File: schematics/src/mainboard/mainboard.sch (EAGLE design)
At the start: 44 parts, among them IC1 TL074P, IC2 TL074P

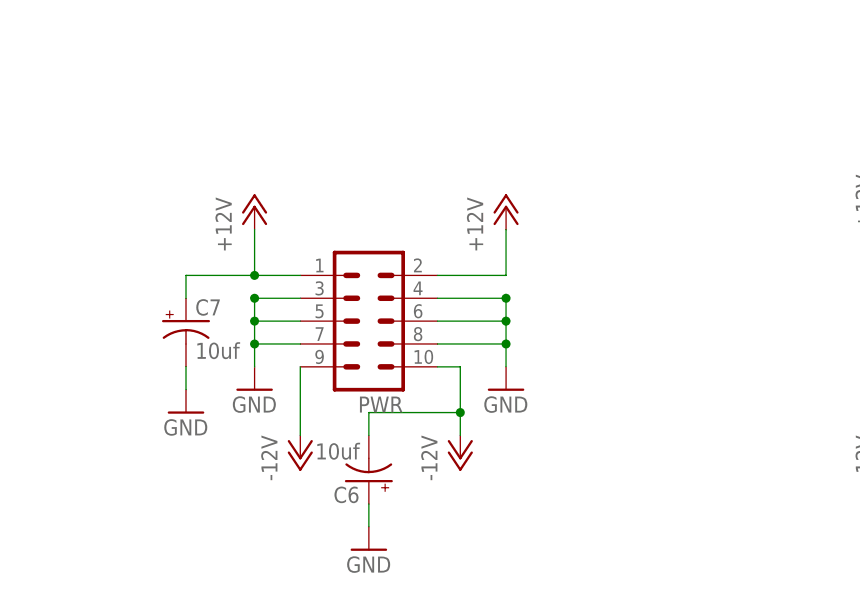
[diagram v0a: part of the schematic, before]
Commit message: Updated Schematics, Fixed Power Socket orientation
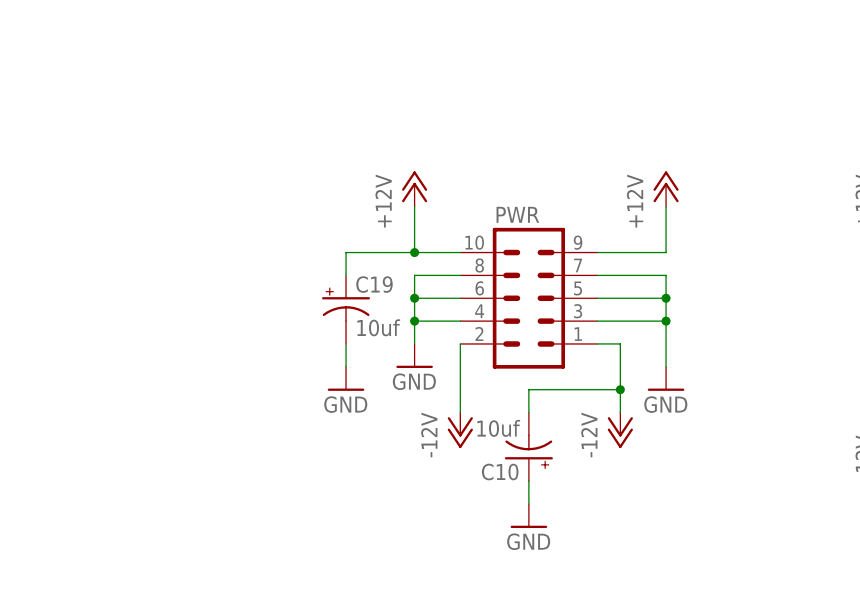
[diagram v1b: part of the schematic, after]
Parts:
- removed C6, C7: 10uf, resistor:CPOL-USE2.5-5
- added C10, C19: 10uf, resistor:CPOL-USE2.5-5
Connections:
- net +12V: now also C19.+, PWR.10, PWR.9; no longer C7.+, PWR.1, PWR.2
- net -12V: now also C10.-, PWR.1, PWR.2; no longer C6.-, PWR.10, PWR.9
- net GND: now also C10.+, C19.-; no longer C6.+, C7.-
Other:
- moved on the sheet: PWR
